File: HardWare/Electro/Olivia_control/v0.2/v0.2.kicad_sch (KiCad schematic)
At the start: 49 parts, among them J1 PROG, J10 Motor_B, J11 I2C, J12 DAC, J13 UART2, J14 TRIAC OUT_A, J15 TRIAC OUT_B, J16 220V IN, J17 In12V, J2 Input1, J3 Input2, J4 Input3, J5 Input4, J6 LED, J7 Reset, J8 SPI, J9 Motor_A, Q1 BTA16-800B, Q2 BTA16-800B, U1 ESP32-WROOM-32D, U2 MOC3041M, U3 MOC3041M, U4 4N25, U5 AMS1117-3.3, U6 HW-613

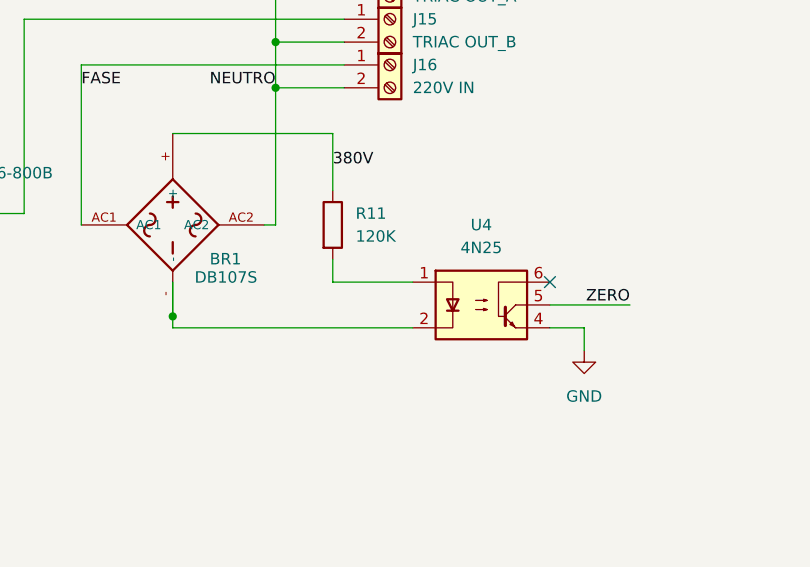
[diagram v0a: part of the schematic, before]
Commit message: replaced 4N25 with TLP181
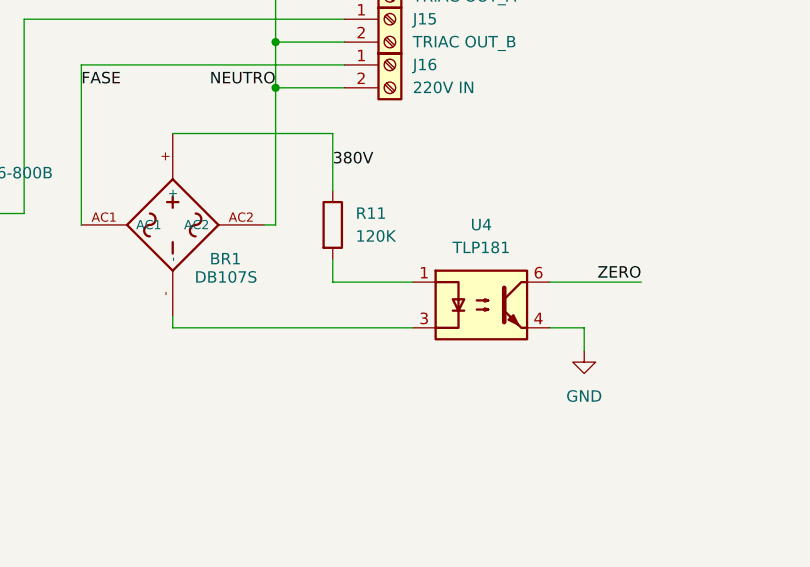
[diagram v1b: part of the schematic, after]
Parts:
- U4: value 4N25 -> TLP181; footprint Package_DIP:SMDIP-6_W9.53mm -> Package_SO:SOIC-4_4.55x3.7mm_P2.54mm; symbol Isolator:4N25 -> Isolator:TLP185
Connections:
- net ZERO: now also U4.6; no longer U4.5
- net at BR1.-: now also U4.3; no longer U4.2
- no-connect marks 7 -> 6
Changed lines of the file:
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@@
 	)
 	(junction
-		(at 175.26 152.4)
-		(diameter 0)
-		(color 0 0 0 0)
-	)
-	(junction
 		(at 186.69 121.92)
 		(diameter 0)
@@
 	)
 	(no_connect
-		(at 217.17 148.59)
-	)
-	(no_connect
 		(at 72.39 69.85)
 	)
@@
 	(wire
 		(pts
-			(xy 179.07 40.64) (xy 179.07 41.91)
+			(xy 175.26 152.4) (xy 175.26 153.67)
 		)
 		(stroke
@@
 	(wire
 		(pts
-			(xy 31.75 160.02) (xy 31.75 162.56)
+			(xy 179.07 40.64) (xy 179.07 41.91)
 		)
 		(stroke
@@
 	(wire
 		(pts
-			(xy 137.16 22.86) (xy 130.81 22.86)
+			(xy 31.75 160.02) (xy 31.75 162.56)
 		)
 		(stroke
@@
 	(wire
 		(pts
-			(xy 24.13 67.31) (xy 34.29 67.31)
+			(xy 137.16 22.86) (xy 130.81 22.86)
 		)
 		(stroke
@@
 	(wire
 		(pts
-			(xy 217.17 151.13) (xy 226.06 151.13)
+			(xy 24.13 67.31) (xy 34.29 67.31)
 		)
 		(stroke
@@
 	(wire
 		(pts
-			(xy 175.26 148.59) (xy 175.26 152.4)
-		)
-		(stroke
-			(width 0)
-			(type default)
-		)
-	)
-	(wire
-		(pts
 			(xy 175.26 153.67) (xy 201.93 153.67)
 		)
@@
 	(wire
 		(pts
-			(xy 175.26 152.4) (xy 175.26 153.67)
-		)
-		(stroke
-			(width 0)
-			(type default)
-		)
-	)
-	(wire
-		(pts
 			(xy 207.01 33.02) (xy 207.01 31.75)
 		)
@@
 	(wire
 		(pts
+			(xy 217.17 148.59) (xy 227.33 148.59)
+		)
+		(stroke
+			(width 0)
+			(type default)
+		)
+	)
+	(wire
+		(pts
 			(xy 182.88 30.48) (xy 182.88 31.75)
 		)
@@
 	)
 	(label "ZERO"
-		(at 226.06 151.13 180)
+		(at 227.33 148.59 180)
 		(effects
 			(font
@@
 	)
 	(symbol
-		(lib_id "Isolator:4N25")
+		(lib_id "Isolator:TLP185")
 		(at 209.55 151.13 0)
 		(unit 1)
@@
 			)
 		)
-		(property "Value" "4N25"
+		(property "Value" "TLP181"
 			(at 209.55 144.78 0)
 			(effects
@@
 			)
 		)
-		(property "Footprint" "Package_DIP:SMDIP-6_W9.53mm"
-			(at 204.47 156.21 0)
+		(property "Footprint" "Package_SO:SOIC-4_4.55x3.7mm_P2.54mm"
+			(at 209.55 158.75 0)
 			(effects
 				(font
@@
 					(italic yes)
 				)
-				(justify left)
 				(hide yes)
 			)
 		)
-		(property "Datasheet" "https://www.vishay.com/docs/83725/4n25.pdf"
+		(property "Datasheet" "https://toshiba.semicon-storage.com/info/docget.jsp?did=11791&prodName=TLP185"
 			(at 209.55 151.13 0)
 			(effects
@@
 			)
 		)
-		(property "Description" "DC Optocoupler Base Connected, Vce 30V, CTR 20%, Viso 2500V, DIP6"
+		(property "Description" "DC Optocoupler, Vce 80V, CTR 50-100%, SOIC-4-6 (MFSOP-4-6)"
 			(at 209.55 151.13 0)
 			(effects
@@
 		(pin "3"
 		)
-		(pin "5"
-		)
 		(pin "1"
 		)
-		(pin "2"
-		)
 		(pin "6"
